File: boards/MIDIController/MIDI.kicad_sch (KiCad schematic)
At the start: 29 parts

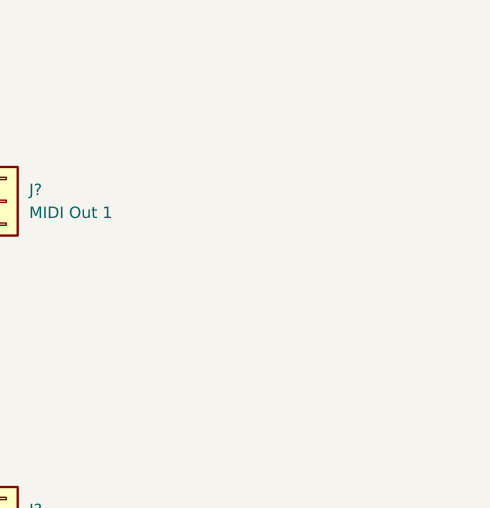
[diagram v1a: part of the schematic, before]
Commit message: Created new signals drawings
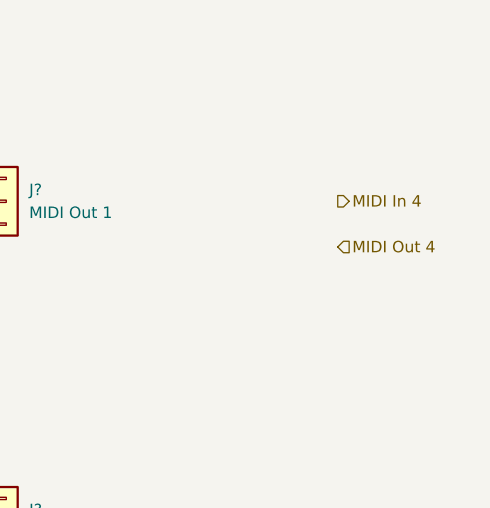
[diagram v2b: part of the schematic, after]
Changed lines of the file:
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@@
     (effects (font (size 1.27 1.27)) (justify right))
+  )
+  (hierarchical_label "MIDI In 4" (shape output) (at 240.03 50.8 0) (fields_autoplaced)
+    (effects (font (size 1.27 1.27)) (justify left))
+  )
+  (hierarchical_label "MIDI Out 4" (shape input) (at 240.03 55.88 0) (fields_autoplaced)
+    (effects (font (size 1.27 1.27)) (justify left))
   )
   (hierarchical_label "MIDI In 2" (shape output) (at 80.01 87.63 180) (fields_autoplaced)

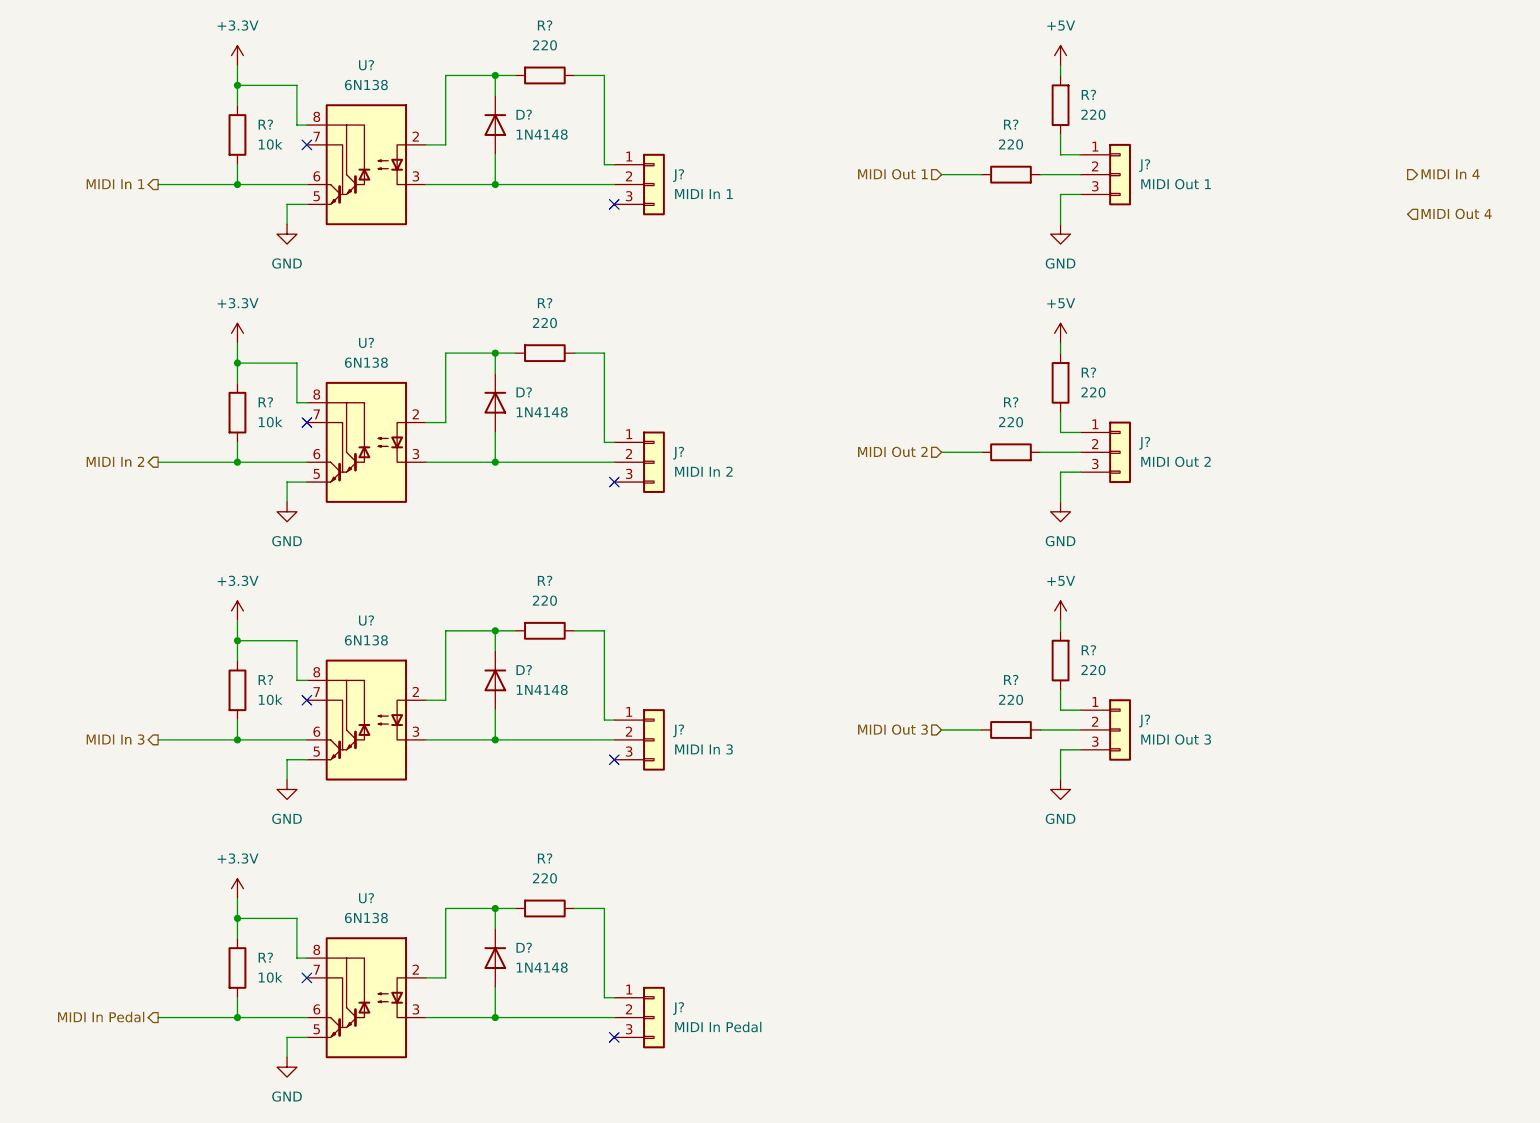
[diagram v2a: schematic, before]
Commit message: Cleanup of PCB sizes and mounthole positions. Moved MIDI connectors to separate board.
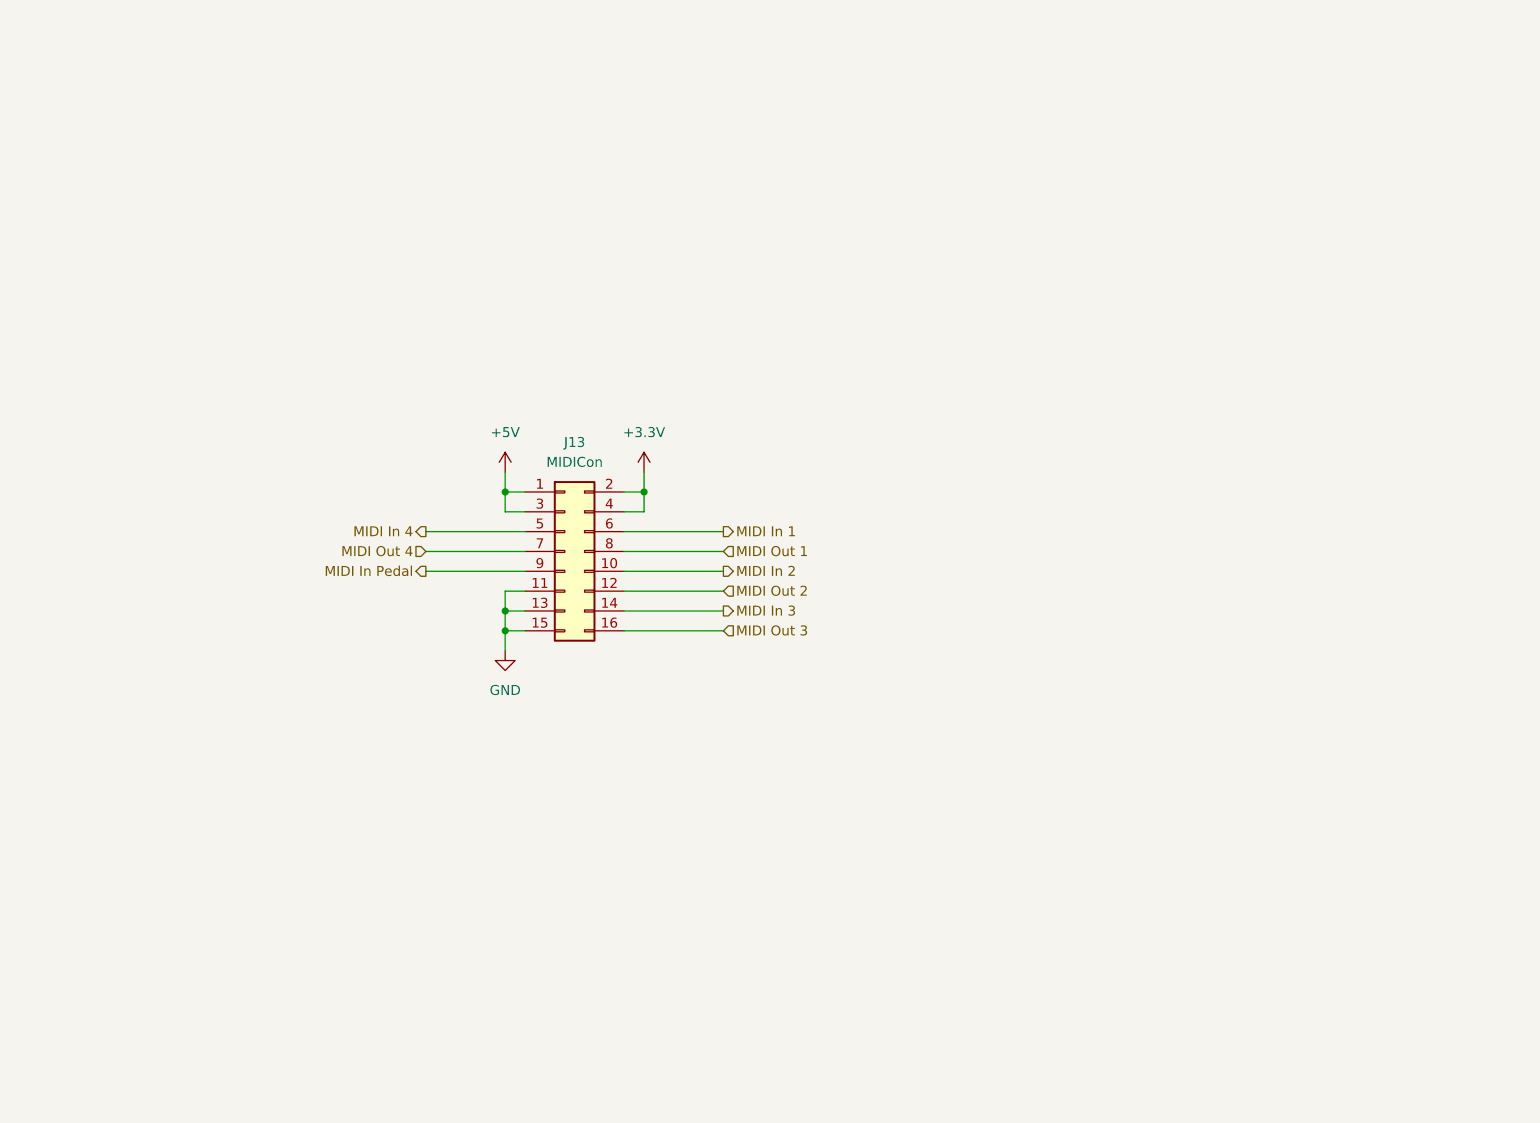
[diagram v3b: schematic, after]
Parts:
- removed D? (x4): 1N4148, Diode_THT:D_DO-35_SOD27_P7.62mm_Horizontal, symbol Diode:1N4148
- removed J?: MIDI In 3, symbol Connector_Generic:Conn_01x03
- removed J?: MIDI Out 1, symbol Connector_Generic:Conn_01x03
- removed J?: MIDI In 1, symbol Connector_Generic:Conn_01x03
- removed J?: MIDI In 2, symbol Connector_Generic:Conn_01x03
- removed J?: MIDI Out 3, symbol Connector_Generic:Conn_01x03
- removed J?: MIDI In Pedal, symbol Connector_Generic:Conn_01x03
- removed J?: MIDI Out 2, symbol Connector_Generic:Conn_01x03
- removed R? (x10): 220, Resistor_THT:R_Axial_DIN0204_L3.6mm_D1.6mm_P2.54mm_Vertical, symbol Device:R
- removed R? (x4): 10k, Resistor_THT:R_Axial_DIN0204_L3.6mm_D1.6mm_P2.54mm_Vertical, symbol Device:R
- removed U? (x4): 6N138, Package_DIP:DIP-8_W7.62mm, symbol Isolator:6N138
- added J13: MIDICon, Connector_IDC:IDC-Header_2x08_P2.54mm_Vertical, symbol Connector_Generic:Conn_02x08_Odd_Even
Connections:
- net +3.3V: now also J13.2 (Pin_2), J13.4 (Pin_4)
- net +5V: now also J13.1 (Pin_1), J13.3 (Pin_3)
- net GND: now also J13.11 (Pin_11), J13.13 (Pin_13), J13.15 (Pin_15)
- net MIDI In 1: now also J13.6 (Pin_6)
- net MIDI In 2: now also J13.10 (Pin_10)
- net MIDI In 3: now also J13.14 (Pin_14)
- net MIDI In 4: now also J13.5 (Pin_5)
- net MIDI In Pedal: now also J13.9 (Pin_9)
- net MIDI Out 1: now also J13.8 (Pin_8)
- net MIDI Out 2: now also J13.12 (Pin_12)
- net MIDI Out 3: now also J13.16 (Pin_16)
- net MIDI Out 4: now also J13.7 (Pin_7)
- no-connect marks 8 -> 0

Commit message: Added Optocoupler and RS232 converter to UART board lines.
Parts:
- removed J13: MIDICon, Connector_IDC:IDC-Header_2x08_P2.54mm_Vertical, symbol Connector_Generic:Conn_02x08_Odd_Even
